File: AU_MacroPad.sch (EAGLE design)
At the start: 95 parts, among them IC1 74HCT1G125DBV, IC3 RP2040_QFN56, SW2 RA SW, SW3 EN11-VSM1AF15, U1 W25Q64, U2 RT9080-3.3, U3 PAM8302, X1 TYPE C, X2 ZJY130-2864KSWLG22, Y1 12MHz/12pF

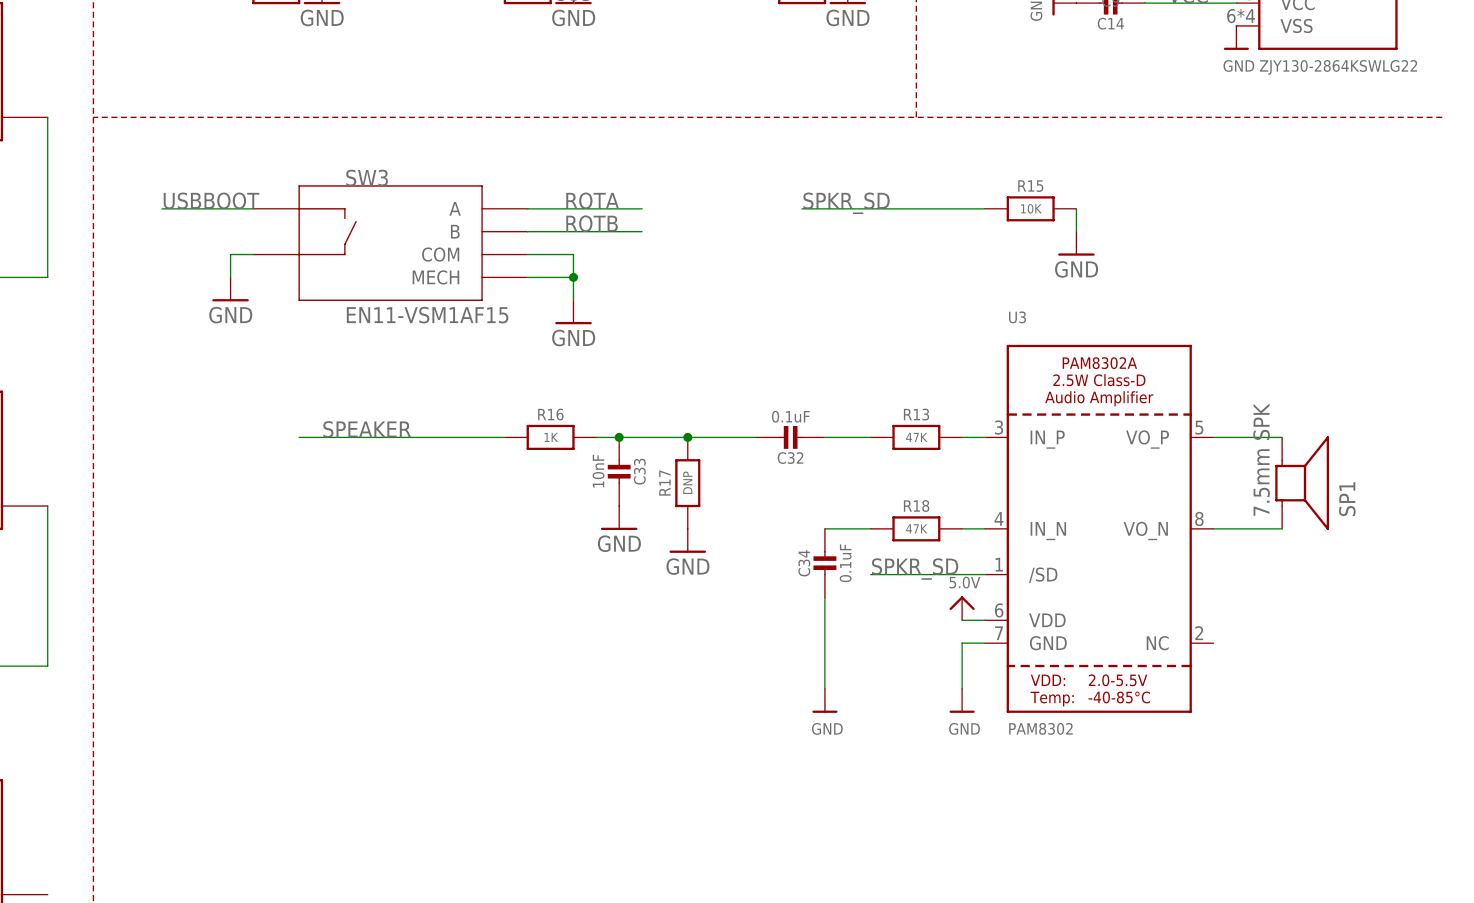
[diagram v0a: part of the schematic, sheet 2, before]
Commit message: Connector rotated 180 degrees and traces re-routed
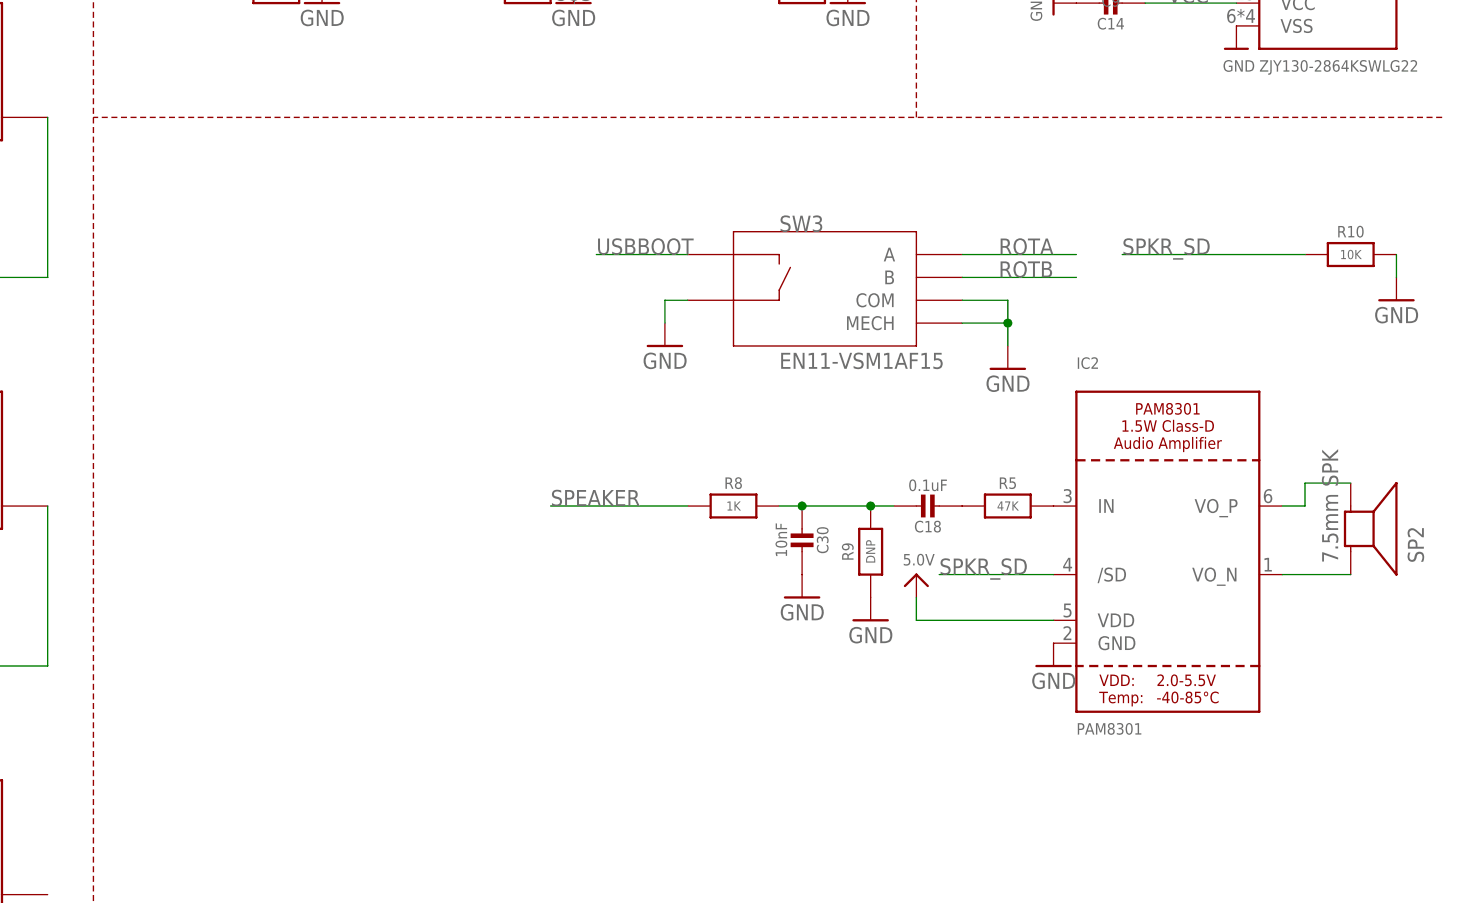
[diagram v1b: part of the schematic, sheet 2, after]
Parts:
- removed C32, C34: 0.1uF, microbuilder:CAP_CERAMIC0603_NO
- removed C33: 10nF, microbuilder:CAP_CERAMIC0603_NO
- removed R13, R18: 47K, microbuilder:RESISTOR_0603_NOOUT
- removed R15: 10K, microbuilder:RESISTOR_0603_NOOUT
- removed R16: 1K, microbuilder:RESISTOR_0603_NOOUT
- removed R17: DNP, microbuilder:RESISTOR_0603_NOOUT
- removed SP1: 7.5mm SPK, microbuilder:SPEAKER_7.5MM
- removed U3: PAM8302, microbuilder:AUDIOAMP_PAM8302A
- added IC2: PAM8301, microbuilder:PAM8301
- added R10: 10K, microbuilder:RESISTOR_0603_NOOUT
- added R5: 47K, microbuilder:RESISTOR_0603_NOOUT
- added R8: 1K, microbuilder:RESISTOR_0603_NOOUT
- added R9: DNP, microbuilder:RESISTOR_0603_NOOUT
- added SP2: 7.5mm SPK, microbuilder:SPEAKER_7.5MM
- C18: value 10uF -> 0.1uF; device microbuilder:CAP_CERAMIC0805-NOOUTLINE -> microbuilder:CAP_CERAMIC0603_NO
- C19, C20: value 22pF -> 12pF
- C30: value 10uF -> 10nF; device microbuilder:CAP_CERAMIC0805-NOOUTLINE -> microbuilder:CAP_CERAMIC0603_NO
- C6: value 10uF -> 10µF
- C8: value 10uF -> 10µF; REV D -> C
- CONN1: device adafruit_electromech:STEMMA_I2C_QT -> microbuilder:STEMMA_I2C_QT
- R2: value 10K -> 10k
- SW2: device adafruit_electromech:SWITCH_SPST_MNT_TACT_RA -> adafruit_electromech:SWITCH_SPST_TACT_RA
- U$1, U$12, U$13, U$2, U$3, U$4, U$40, U$41, U$42, U$43, U$5, U$6: XOFFSET -0.75 -> (none)
- U1: value W25Q64 -> GD25x16
- U2: value RT9080-3.3 -> AP2112K-3.3; device adafruit_power:VREG_SOT23-5 -> microbuilder:VREG_SOT23-5; JLC_ROTATION 0 -> (none)
- Y1: value 12MHz/12pF -> 12MHZ
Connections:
- removed net IN+: R13.2, U3.IN_P
- removed net IN-: R18.2, U3.IN_N
- removed net N$28: C32.2, R13.1
- removed net N$29: C32.1, C33.2, R16.2, R17.2
- removed net N$30: C34.1, R18.1
- removed net N$31: SP1.-, U3.VO_P
- removed net N$32: SP1.+, U3.VO_N
- new net N$100: C18.1, C30.2, R8.2, R9.2
- new net N$22: IC2.VO_N, SP2.+
- new net N$27: IC2.VO_P, SP2.-
- new net N$8: C18.2, R5.1
- new net N$9: IC2.IN, R5.2
- net 5.0V: now also IC2.VDD; no longer C18.2, C30.2, U3.VDD
- net GND: now also IC2.GND, R10.2, R9.1; no longer C18.1, C33.1, C34.2, R15.2, R17.1, U3.GND
- net SPEAKER: now also R8.1; no longer R16.1
- net SPKR_SD: now also IC2./SD, R10.1; no longer R15.1, U3./SD
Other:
- moved on the sheet: SW3

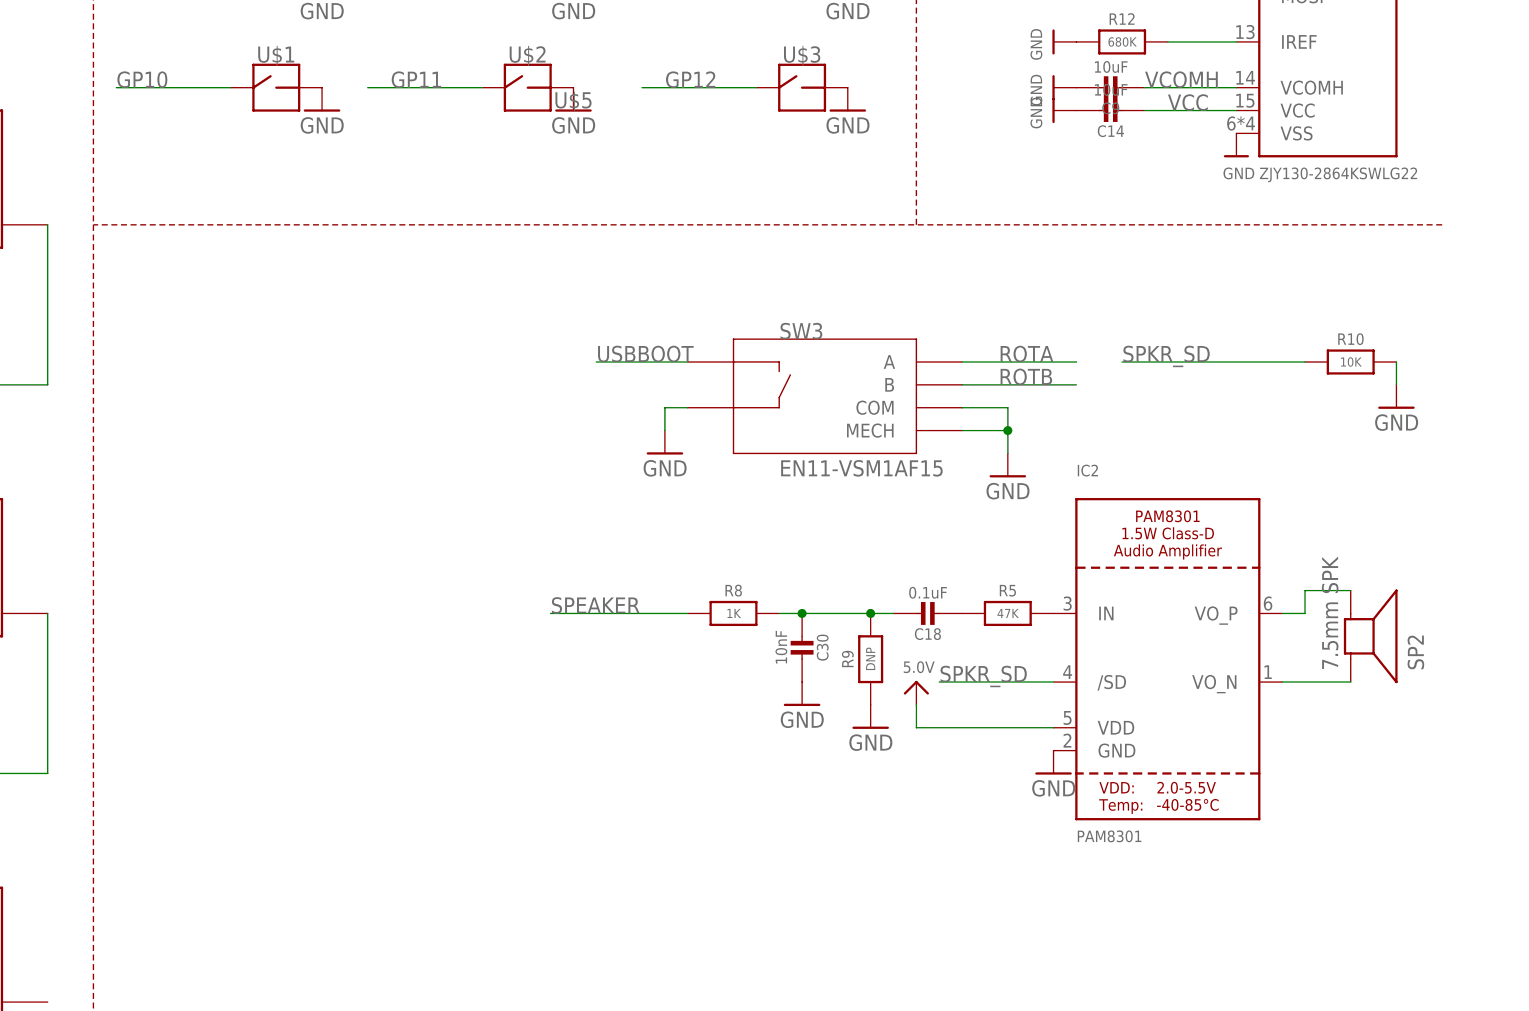
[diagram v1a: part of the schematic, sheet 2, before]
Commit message: Add files via upload
Built from Limor's files. Rotated connector 180 degrees and re-routed.
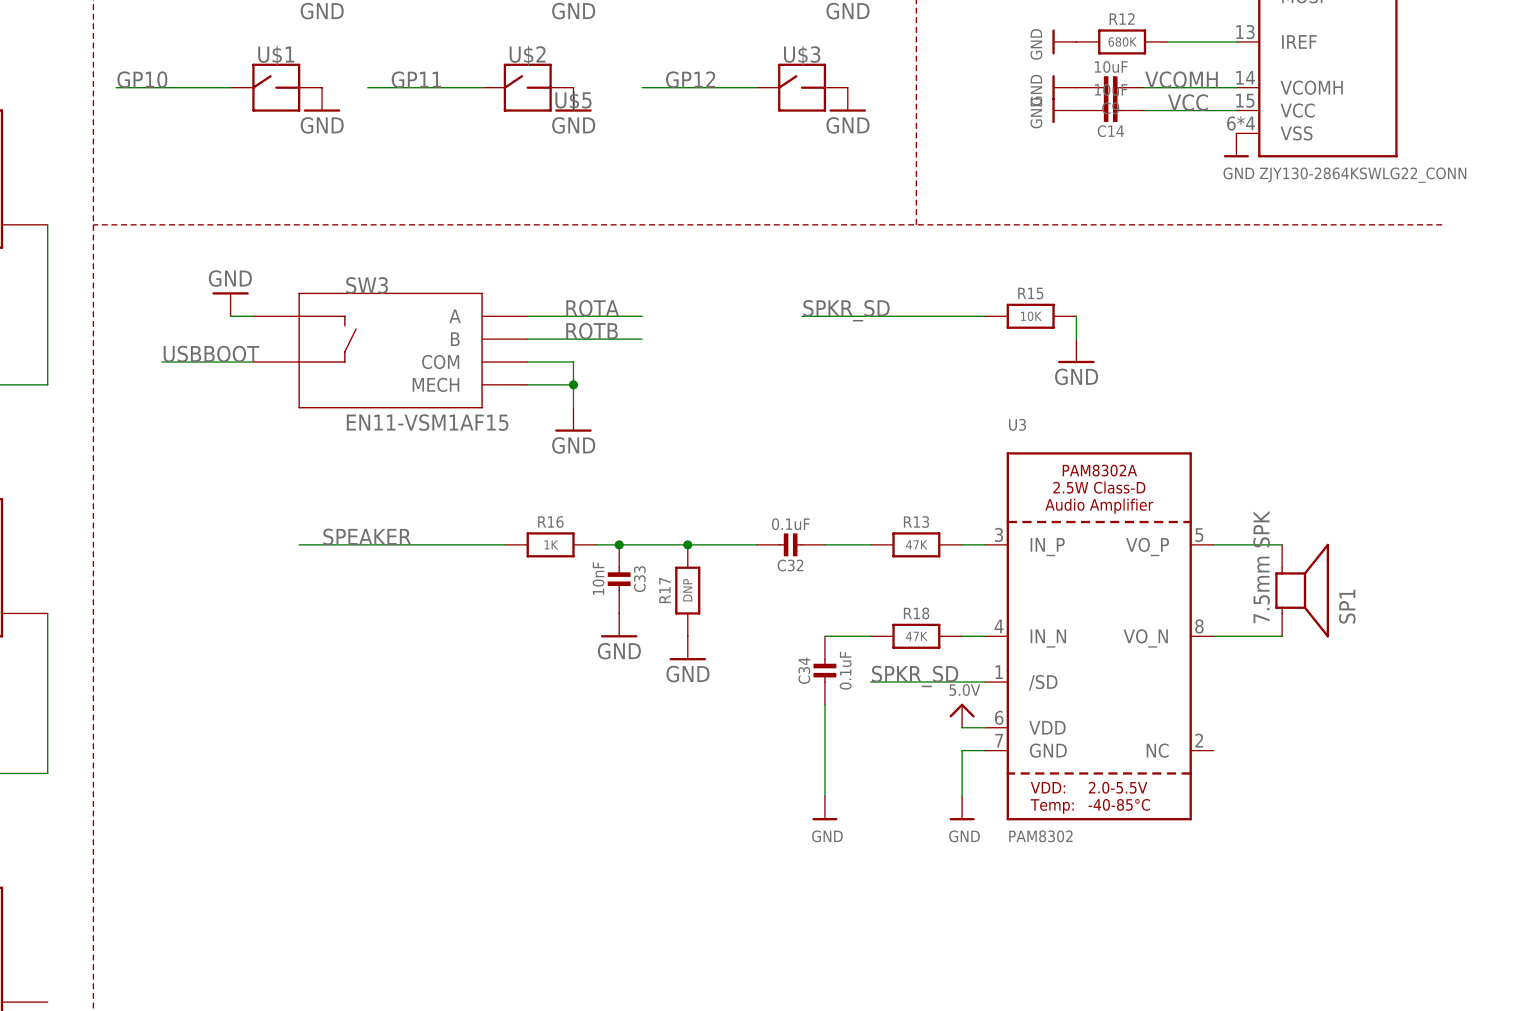
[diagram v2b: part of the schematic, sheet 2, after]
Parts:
- removed IC2: PAM8301, microbuilder:PAM8301
- removed R10: 10K, microbuilder:RESISTOR_0603_NOOUT
- removed R5: 47K, microbuilder:RESISTOR_0603_NOOUT
- removed R8: 1K, microbuilder:RESISTOR_0603_NOOUT
- removed R9: DNP, microbuilder:RESISTOR_0603_NOOUT
- removed SP2: 7.5mm SPK, microbuilder:SPEAKER_7.5MM
- added C32, C34: 0.1uF, microbuilder:CAP_CERAMIC0603_NO
- added C33: 10nF, microbuilder:CAP_CERAMIC0603_NO
- added R13, R18: 47K, microbuilder:RESISTOR_0603_NOOUT
- added R15: 10K, microbuilder:RESISTOR_0603_NOOUT
- added R16: 1K, microbuilder:RESISTOR_0603_NOOUT
- added R17: DNP, microbuilder:RESISTOR_0603_NOOUT
- added SP1: 7.5mm SPK, microbuilder:SPEAKER_7.5MM
- added U$79, U$83: FIDUCIAL_1MM, microbuilder:FIDUCIAL_1MM
- added U3: PAM8302, microbuilder:AUDIOAMP_PAM8302A
- C18: value 0.1uF -> 10uF; device microbuilder:CAP_CERAMIC0603_NO -> microbuilder:CAP_CERAMIC0805-NOOUTLINE
- C19, C20: value 12pF -> 22pF
- C30: value 10nF -> 10uF; device microbuilder:CAP_CERAMIC0603_NO -> microbuilder:CAP_CERAMIC0805-NOOUTLINE
- C6: value 10µF -> 10uF
- C8: value 10µF -> 10uF; REV C -> D
- CONN1: device microbuilder:STEMMA_I2C_QT -> adafruit_electromech:STEMMA_I2C_QT
- R2: value 10k -> 10K
- SW2: device adafruit_electromech:SWITCH_SPST_TACT_RA -> adafruit_electromech:SWITCH_SPST_MNT_TACT_RA
- U$1, U$12, U$13, U$2, U$3, U$4, U$40, U$41, U$42, U$43, U$5, U$6: XOFFSET (none) -> -0.75
- U1: value GD25x16 -> W25Q64
- U2: value AP2112K-3.3 -> RT9080-3.3; device microbuilder:VREG_SOT23-5 -> adafruit_power:VREG_SOT23-5; JLC_ROTATION (none) -> 0
- X2: value ZJY130-2864KSWLG22 -> ZJY130-2864KSWLG22_CONN; device adafruit_display:ZJY130-2864KSWLG22 -> adafruit_display:ZJY130-2864KSWLG22_CONN
- Y1: value 12MHZ -> 12MHz/12pF
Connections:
- removed net N$100: C18.1, C30.2, R8.2, R9.2
- removed net N$22: IC2.VO_N, SP2.+
- removed net N$27: IC2.VO_P, SP2.-
- removed net N$8: C18.2, R5.1
- removed net N$9: IC2.IN, R5.2
- new net IN+: R13.2, U3.IN_P
- new net IN-: R18.2, U3.IN_N
- new net N$28: C32.2, R13.1
- new net N$29: C32.1, C33.2, R16.2, R17.2
- new net N$30: C34.1, R18.1
- new net N$31: SP1.-, U3.VO_P
- new net N$32: SP1.+, U3.VO_N
- net 5.0V: now also C18.2, C30.2, U3.VDD; no longer IC2.VDD
- net GND: now also C18.1, C33.1, C34.2, R15.2, R17.1, SW3.D, U3.GND; no longer IC2.GND, R10.2, R9.1, SW3.E
- net SPEAKER: now also R16.1; no longer R8.1
- net SPKR_SD: now also R15.1, U3./SD; no longer IC2./SD, R10.1
- net USBBOOT: now also SW3.E; no longer SW3.D
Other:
- moved on the sheet: SW3
